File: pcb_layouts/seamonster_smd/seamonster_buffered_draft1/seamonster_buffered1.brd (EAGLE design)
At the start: 172.5 x 106.5 mm, 122 parts, among them IC1 7808DT, IC2 4051D, IC3 4051D, IC4 DG408DY, IC5 4046D, IC6 40106D, IC7 4070D, IC8 4046D, IC9 4040D, Q1 THONKICONNNEW, Q2 THONKICONNNEW, Q3 THONKICONNNEW, Q4 THONKICONNNEW, Q5 THONKICONNNEW, Q6 THONKICONNNEW, SW1 SPDT ON-ON, SW2 SPDT ON-ON, SW3 SPDT ON-ON, SW4 SPDT ON-ON, U1 TL084, U2 TL084, U3 TL084

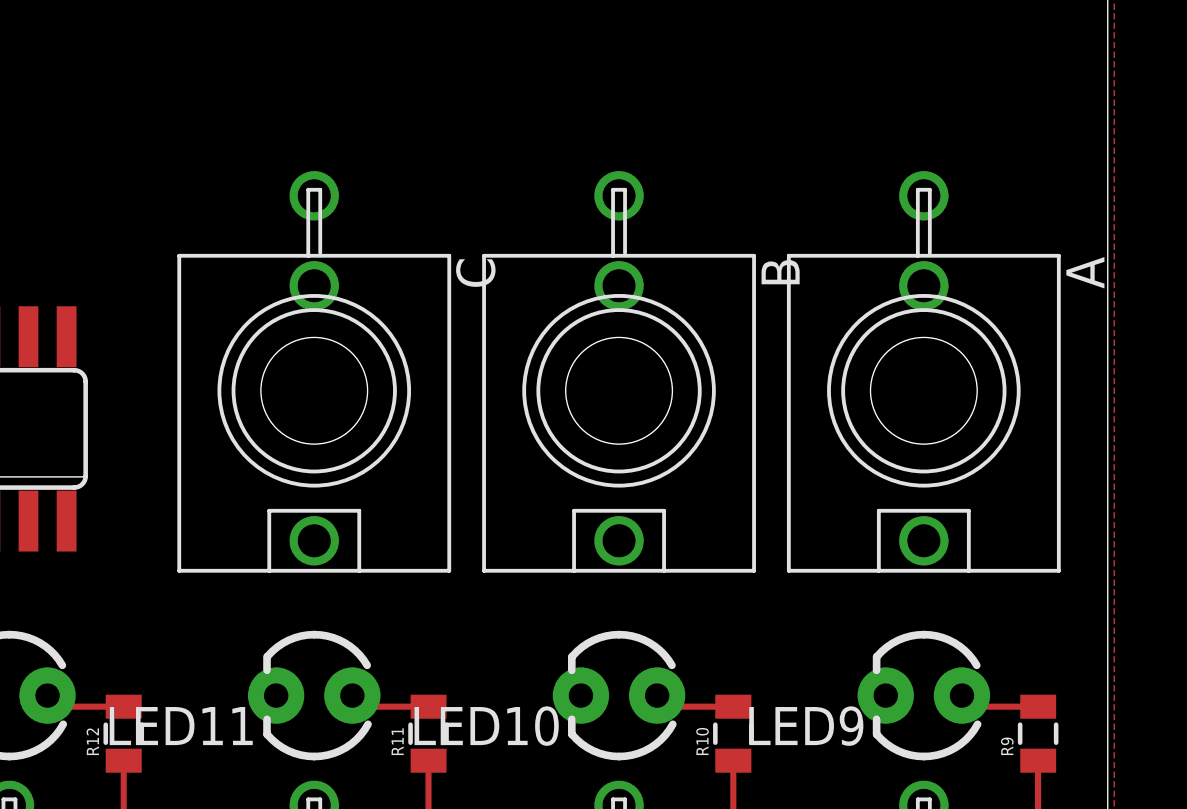
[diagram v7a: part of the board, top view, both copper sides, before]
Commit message: added jumpers for normalled ABC bus operation
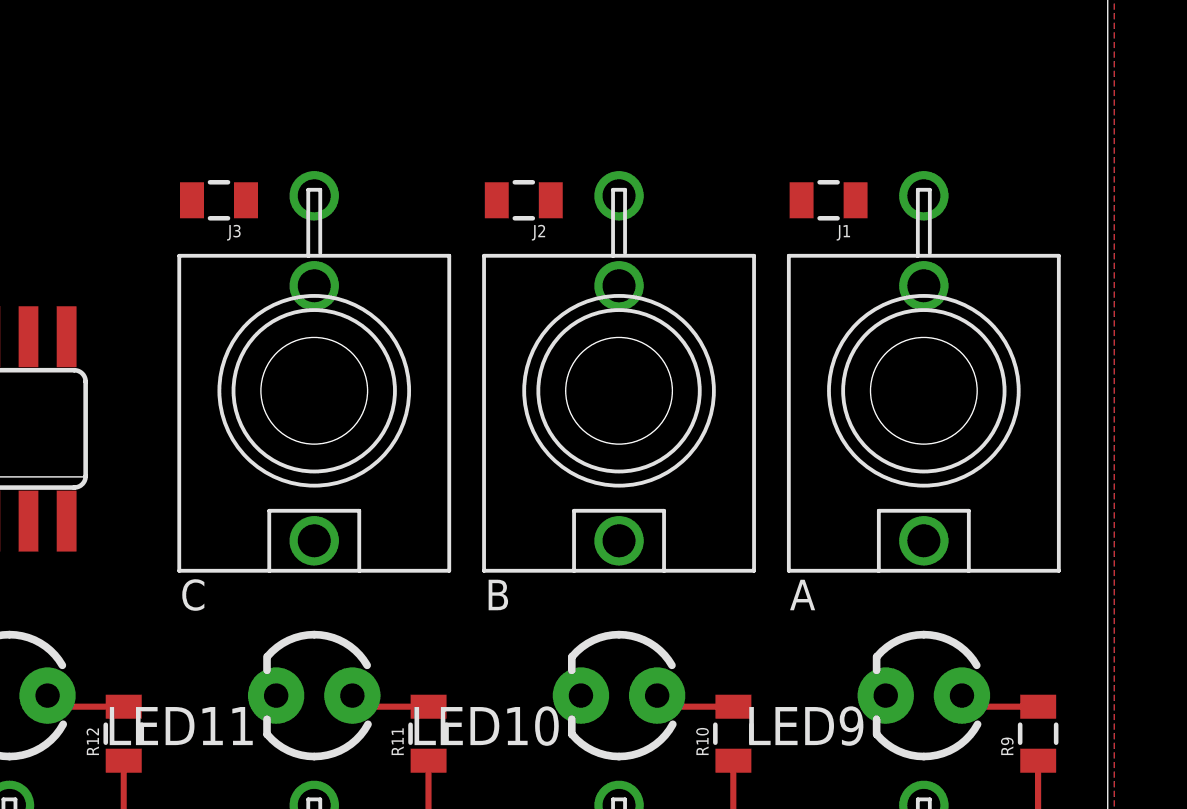
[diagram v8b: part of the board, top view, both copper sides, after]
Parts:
- added J1, J2, J3: (no value), SparkFun-Resistors:0805
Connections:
- net N$2 renamed MUX1
- net N$3 renamed MUX2
- net N$4 renamed MUX3
- net N$5 renamed MUX4
- net N$6 renamed MUX5
- net N$7 renamed MUX6
- net N$8 renamed MUX7
- net N$9 renamed MUX8
- new net N$34: A.P$2_SWITCH, J1.1
- new net N$37: B.P$2_SWITCH, J2.1
- new net N$76: C.P$2_SWITCH, J3.1
- net Q1: now also J1.2
- net Q2: now also J2.2
- net Q3: now also J3.2
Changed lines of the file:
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@@
 </autorouter>
 <elements>
-<element name="A" library="MusicThingModular" package="WQP-PJ301M-12_JACK" value="THONKICONNNEW" x="166.37" y="39.37" rot="R180"/>
-<element name="B" library="MusicThingModular" package="WQP-PJ301M-12_JACK" value="THONKICONNNEW" x="156.21" y="39.37" rot="R180"/>
-<element name="C" library="MusicThingModular" package="WQP-PJ301M-12_JACK" value="THONKICONNNEW" x="146.05" y="39.37" rot="R180"/>
+<element name="A" library="MusicThingModular" package="WQP-PJ301M-12_JACK" value="THONKICONNNEW" x="166.37" y="39.37" smashed="yes" rot="R180">
+<attribute name="NAME" x="161.8996" y="32.0548" size="1.016" layer="21" font="vector"/>
+</element>
+<element name="B" library="MusicThingModular" package="WQP-PJ301M-12_JACK" value="THONKICONNNEW" x="156.21" y="39.37" smashed="yes" rot="R180">
+<attribute name="NAME" x="151.7396" y="32.0548" size="1.016" layer="21" font="vector"/>
+</element>
+<element name="C" library="MusicThingModular" package="WQP-PJ301M-12_JACK" value="THONKICONNNEW" x="146.05" y="39.37" smashed="yes" rot="R180">
+<attribute name="NAME" x="141.5796" y="32.0548" size="1.016" layer="21" font="vector"/>
+</element>
 <element name="C1" library="SparkFun-Capacitors" package="CPOL-RADIAL-10UF-25V" value="47µF" x="107.95" y="29.845" rot="MR0"/>
 <element name="C2" library="SparkFun-Capacitors" package="CPOL-RADIAL-10UF-25V" value="47µF" x="90.17" y="29.845" rot="R180"/>
@@
 </element>
 <element name="IC1" library="linear" library_urn="urn:adsk.eagle:library:262" package="TO252" value="7808DT" x="120.65" y="50.8"/>
+<element name="J1" library="SparkFun-Resistors" package="0805" value="" x="163.195" y="45.72" rot="R180"/>
+<element name="J2" library="SparkFun-Resistors" package="0805" value="" x="153.035" y="45.72" rot="R180"/>
+<element name="J3" library="SparkFun-Resistors" package="0805" value="" x="142.875" y="45.72" rot="R180"/>
 </elements>
 <signals>
@@
 <wire x1="5.08" y1="39.9034" x2="28.575" y2="38.1" width="0" layer="19" extent="1-1"/>
 </signal>
-<signal name="N$2">
+<signal name="MUX1">
 <contactref element="MUX1" pad="P$1_TIP"/>
 <contactref element="IC4" pad="4"/>
 <wire x1="10.16" y1="87.55" x2="137.6934" y2="94.615" width="0" layer="19" extent="1-1"/>
 </signal>
-<signal name="N$3">
+<signal name="MUX2">
 <contactref element="MUX2" pad="P$1_TIP"/>
 <contactref element="IC4" pad="5"/>
 <wire x1="29.21" y1="87.55" x2="137.6934" y2="95.885" width="0" layer="19" extent="1-1"/>
 </signal>
-<signal name="N$4">
+<signal name="MUX3">
 <contactref element="MUX3" pad="P$1_TIP"/>
 <contactref element="IC4" pad="6"/>
 <wire x1="48.26" y1="87.55" x2="137.6934" y2="97.155" width="0" layer="19" extent="1-1"/>
 </signal>
-<signal name="N$5">
+<signal name="MUX4">
 <contactref element="MUX4" pad="P$1_TIP"/>
 <contactref element="IC4" pad="7"/>
@@
 <wire x1="113.03" y1="90.805" x2="137.6934" y2="98.425" width="0" layer="19" extent="1-1"/>
 </signal>
-<signal name="N$6">
+<signal name="MUX5">
 <contactref element="MUX5" pad="P$1_TIP"/>
 <contactref element="IC4" pad="12"/>
@@
 <wire x1="133.35" y1="95.885" x2="131.5466" y2="95.885" width="0.2032" layer="1"/>
 </signal>
-<signal name="N$7">
+<signal name="MUX6">
 <contactref element="MUX6" pad="P$1_TIP"/>
 <contactref element="IC4" pad="11"/>
@@
 <wire x1="133.985" y1="97.155" x2="131.5466" y2="97.155" width="0.2032" layer="1"/>
 </signal>
-<signal name="N$8">
+<signal name="MUX7">
 <contactref element="MUX7" pad="P$1_TIP"/>
 <contactref element="IC4" pad="10"/>
@@
 <wire x1="133.985" y1="98.425" x2="131.5466" y2="98.425" width="0.2032" layer="1"/>
 </signal>
-<signal name="N$9">
+<signal name="MUX8">
 <contactref element="MUX8" pad="P$1_TIP"/>
 <contactref element="IC4" pad="9"/>
@@
 <wire x1="170.18" y1="27.04" x2="170.18" y2="17.86" width="0.2032" layer="1"/>
 <wire x1="170.18" y1="17.86" x2="166.37" y2="14.05" width="0.2032" layer="1" curve="-90"/>
+<contactref element="J1" pad="2"/>
 <wire x1="170.18" y1="27.04" x2="137.795" y2="41.1734" width="0" layer="19" extent="1-1"/>
+<wire x1="162.295" y1="45.72" x2="137.795" y2="41.1734" width="0" layer="19" extent="1-1"/>
 </signal>
 <signal name="Q2">
@@
 <wire x1="160.02" y1="27.04" x2="160.02" y2="17.86" width="0.2032" layer="1"/>
 <wire x1="160.02" y1="17.86" x2="156.21" y2="14.05" width="0.2032" layer="1" curve="-90"/>
+<contactref element="J2" pad="2"/>
 <wire x1="160.02" y1="27.04" x2="136.525" y2="35.0266" width="0" layer="19" extent="1-1"/>
+<wire x1="152.135" y1="45.72" x2="136.525" y2="35.0266" width="0" layer="19" extent="1-1"/>
 </signal>
 <signal name="Q3">
@@
 <wire x1="149.86" y1="27.04" x2="149.86" y2="17.86" width="0.2032" layer="1"/>
 <wire x1="149.86" y1="17.86" x2="146.05" y2="14.05" width="0.2032" layer="1" curve="-90"/>
+<contactref element="J3" pad="2"/>
 <wire x1="149.86" y1="27.04" x2="135.255" y2="35.0266" width="0" layer="19" extent="1-1"/>
+<wire x1="141.975" y1="45.72" x2="135.255" y2="35.0266" width="0" layer="19" extent="1-1"/>
 </signal>
 <signal name="Q4">
@@
 <wire x1="6.35" y1="25.55" x2="16.51" y2="25.55" width="0" layer="19" extent="1-1"/>
 </signal>
+<signal name="N$34">
+<contactref element="A" pad="P$2_SWITCH"/>
+<contactref element="J1" pad="1"/>
+<wire x1="164.095" y1="45.72" x2="166.37" y2="42.87" width="0" layer="19" extent="1-1"/>
+</signal>
+<signal name="N$37">
+<contactref element="B" pad="P$2_SWITCH"/>
+<contactref element="J2" pad="1"/>
+<wire x1="153.935" y1="45.72" x2="156.21" y2="42.87" width="0" layer="19" extent="1-1"/>
+</signal>
+<signal name="N$76">
+<contactref element="C" pad="P$2_SWITCH"/>
+<contactref element="J3" pad="1"/>
+<wire x1="143.775" y1="45.72" x2="146.05" y2="42.87" width="0" layer="19" extent="1-1"/>
+</signal>
 </signals>
